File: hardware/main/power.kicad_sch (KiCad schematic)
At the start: 37 parts, among them Q1 SSM3J338R, Q10 SSM3J338R, Q11 BC817, Q2 BCP53, Q3 SSM3J338R, Q4 BC817, Q5 SSM3J338R, Q6 BC807, Q7 BC817, Q8 SSM3J338R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

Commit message: Exchange the battery connector for a JST XH connector
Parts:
- BT1, BT2: footprint Connector_PinHeader_2.54mm:PinHeader_1x02_P2.54mm_Horizontal -> Connector_JST:JST_XH_S2B-XH-A_1x02_P2.50mm_Horizontal
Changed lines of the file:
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@@
     (property "Reference" "BT1" (id 0) (at 216.9352 59.69 90))
     (property "Value" "NiMH" (id 1) (at 214.637 59.69 90))
-    (property "Footprint" "Connector_PinHeader_2.54mm:PinHeader_1x02_P2.54mm_Horizontal" (id 2) (at 210.82 58.166 90)
+    (property "Footprint" "Connector_JST:JST_XH_S2B-XH-A_1x02_P2.50mm_Horizontal" (id 2) (at 210.82 58.166 90)
       (effects (font (size 1.27 1.27)) hide)
     )
@@
     (property "Reference" "BT2" (id 0) (at 216.9352 72.39 90))
     (property "Value" "NiMH" (id 1) (at 214.637 72.39 90))
-    (property "Footprint" "Connector_PinHeader_2.54mm:PinHeader_1x02_P2.54mm_Horizontal" (id 2) (at 210.82 70.866 90)
+    (property "Footprint" "Connector_JST:JST_XH_S2B-XH-A_1x02_P2.50mm_Horizontal" (id 2) (at 210.82 70.866 90)
       (effects (font (size 1.27 1.27)) hide)
     )

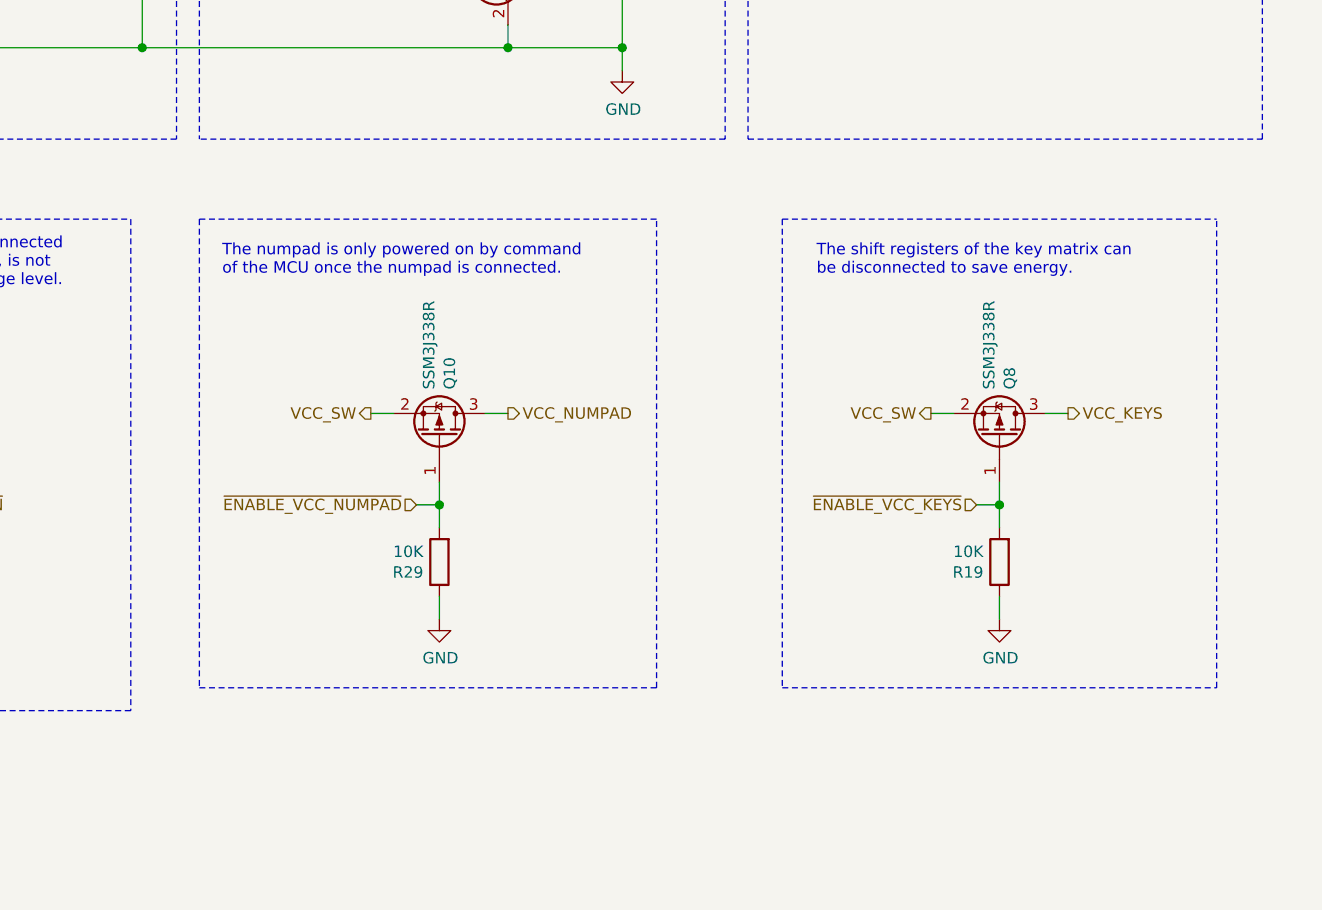
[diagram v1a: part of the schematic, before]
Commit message: hardware: Change key matrix/numpad voltage to be off by default.
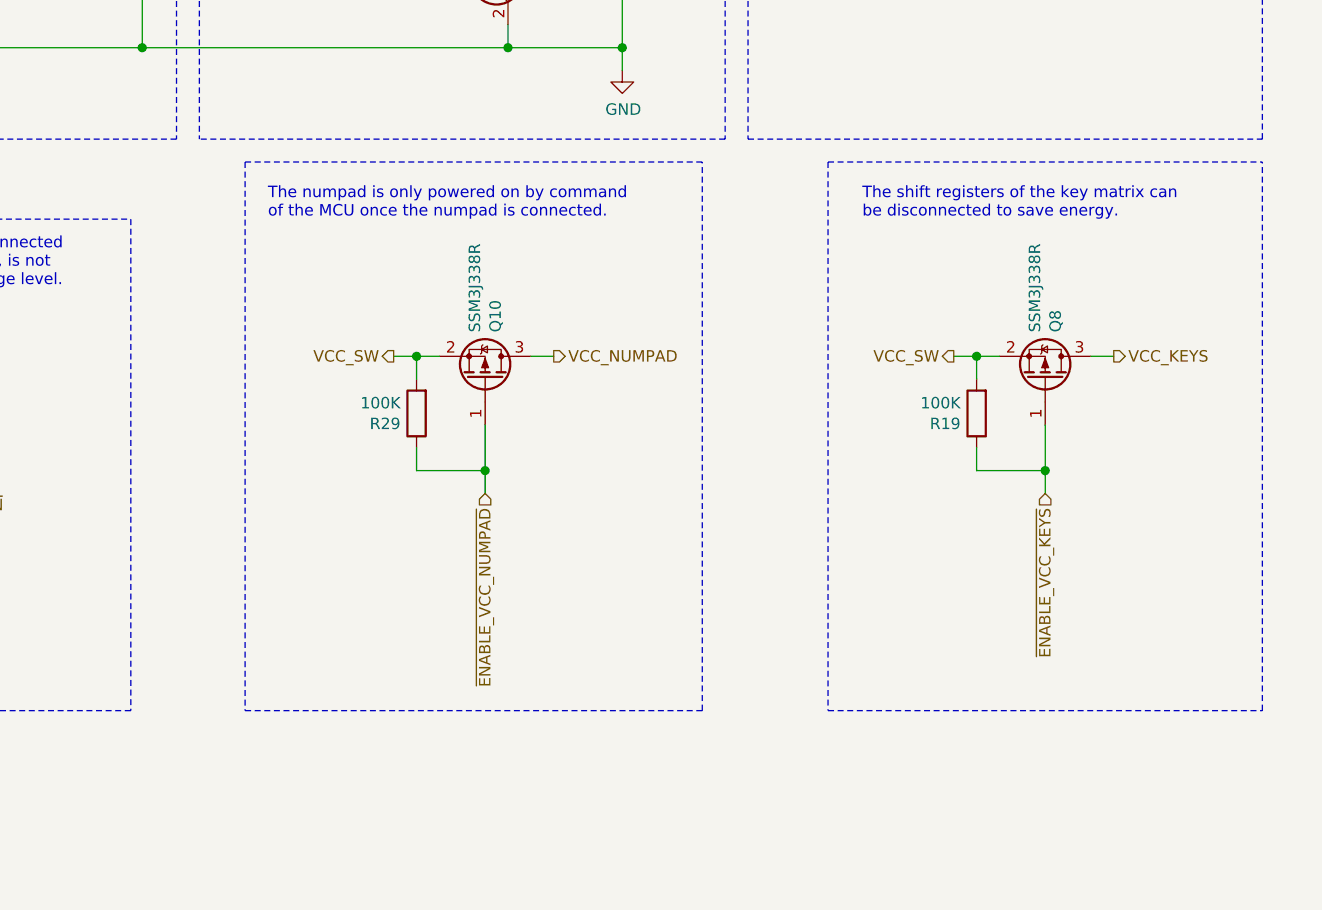
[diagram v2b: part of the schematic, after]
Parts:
- R19, R29: value 10K -> 100K
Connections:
- net GND: no longer R19.1, R29.1
- net VCC_SW: now also R19.2, R29.2
- net ~ENABLE_VCC_KEYS: now also R19.1; no longer R19.2
- net ~ENABLE_VCC_NUMPAD: now also R29.1; no longer R29.2
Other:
- moved on the sheet: Q10, Q8, R19, R29

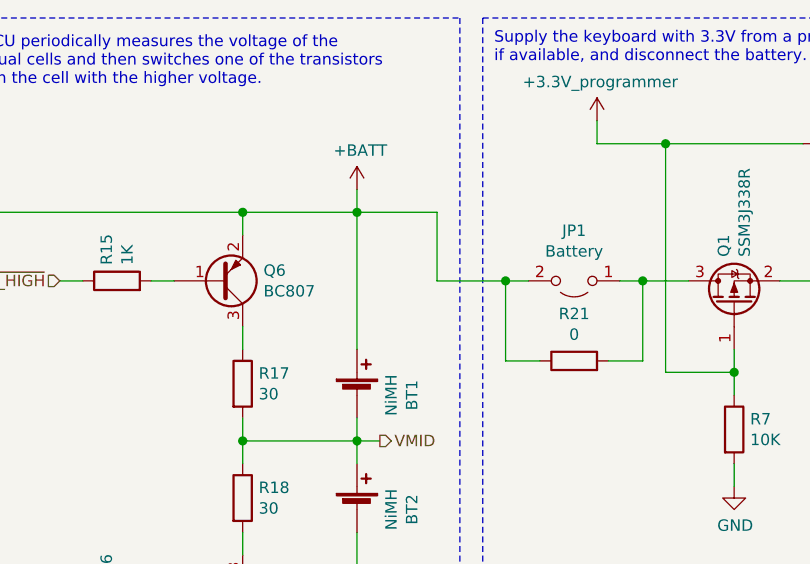
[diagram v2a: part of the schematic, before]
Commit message: Main: Add a fuse to BATT+
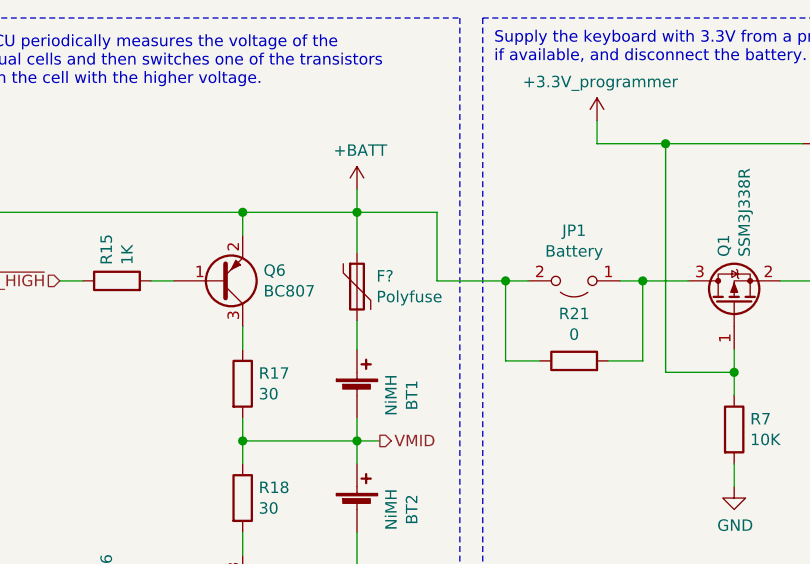
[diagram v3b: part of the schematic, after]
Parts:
- added F?: Polyfuse, Fuse:Fuse_1210_3225Metric_Pad1.42x2.65mm_HandSolder, symbol Device:Polyfuse
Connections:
- net +BATT: now also F?.1; no longer BT1.1 (+)
- new net: BT1.1 (+), F?.2
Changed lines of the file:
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@@
     (stroke (width 0) (type solid) (color 0 0 0 0))
   )
-  (wire (pts (xy 210.82 39.37) (xy 210.82 54.61))
+  (wire (pts (xy 210.82 39.37) (xy 210.82 43.815))
     (stroke (width 0) (type solid) (color 0 0 0 0))
   )
   (wire (pts (xy 210.82 39.37) (xy 219.71 39.37))
+    (stroke (width 0) (type solid) (color 0 0 0 0))
+  )
+  (wire (pts (xy 210.82 51.435) (xy 210.82 54.61))
     (stroke (width 0) (type solid) (color 0 0 0 0))
   )
@@
       (effects (font (size 1.27 1.27)) hide)
     )
+    (pin "1")
+    (pin "2")
+  )
+  (symbol (lib_id "Device:Polyfuse") (at 210.82 47.625 0) (unit 1)
+    (in_bom yes) (on_board yes)
+    (property "Reference" "F?" (id 0) (at 212.9791 46.4756 0)
+      (effects (font (size 1.27 1.27)) (justify left))
+    )
+    (property "Value" "Polyfuse" (id 1) (at 212.9791 48.7743 0)
+      (effects (font (size 1.27 1.27)) (justify left))
+    )
+    (property "Footprint" "Fuse:Fuse_1210_3225Metric_Pad1.42x2.65mm_HandSolder" (id 2) (at 212.09 52.705 0)
+      (effects (font (size 1.27 1.27)) (justify left) hide)
+    )
+    (property "Datasheet" "https://www.mouser.de/datasheet/2/643/ds_CP_0zch_series-1664103.pdf" (id 3) (at 210.82 47.625 0)
+      (effects (font (size 1.27 1.27)) hide)
+    )
+    (property "Mouser" " 530-0ZCH0075FF2G " (id 4) (at 210.82 47.625 0)
+      (effects (font (size 1.27 1.27)) hide)
+    )
+    (property "Part Name" "0ZCH0075FF2G" (id 5) (at 210.82 47.625 0)
+      (effects (font (size 1.27 1.27)) hide)
+    )

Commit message: Main: Review of schematics
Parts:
- C10, C11, C8, C9: Mouser 963-LMK212F106ZG-T -> 187-CL21A106KOQNNNG; Part Name Taiyo Yuden LMK212F106ZG-T -> Samsung CL21A106KOQNNNG
- D48: Mouser 241-BAT54A_R1_00001 -> 241-BAT54C_R1_00001; Part Name BAT54A -> BAT54C_R1_00001
- F1: renamed from F?; Mouser 530-0ZCH0075FF2G -> 530-0ZCH0075FF2G; Part Name 0ZCH0075FF2G -> bel 0ZCH0075FF2G
- Q11, Q4, Q7: Mouser (none) -> 771-BC817-40-T/R; Part Name (none) -> Nexperia BC817-40,215
- Q6: Mouser (none) -> 771-BC807-40LR; Part Name (none) -> Nexperia BC807-40LR
- U7: footprint (none) -> Package_SO:TSSOP-8_4.4x3mm_P0.65mm; Mouser (none) -> 595-LM358PW; Part Name (none) -> LM358PW
- U7: Mouser 595-LM358PW -> 595-LM358PW
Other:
- note removed: "TODO: polarity-proof connectors for the batteries"
